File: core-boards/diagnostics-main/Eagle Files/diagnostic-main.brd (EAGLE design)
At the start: 79.2 x 84.8 mm, 50 parts, among them J1 A118090TR-ND, J2 3M15451-ND, J4 B2PS-VH(LF)(SN), Q1 16 MHz, U1 ATMEGA2560-16AU, U2 296-38653-1-ND, U3 MCP2551T-I/SN, U4 LM1085ISX-5.0/NOPB, U6 TXB0106PWR, U8 LP2985IM5X-3.3/NOPB, X1 22-23-2031, X2 B6B-EH-A(LF)(SN), X3 CC1101, X5 22-23-2031, X8 WM4803-ND

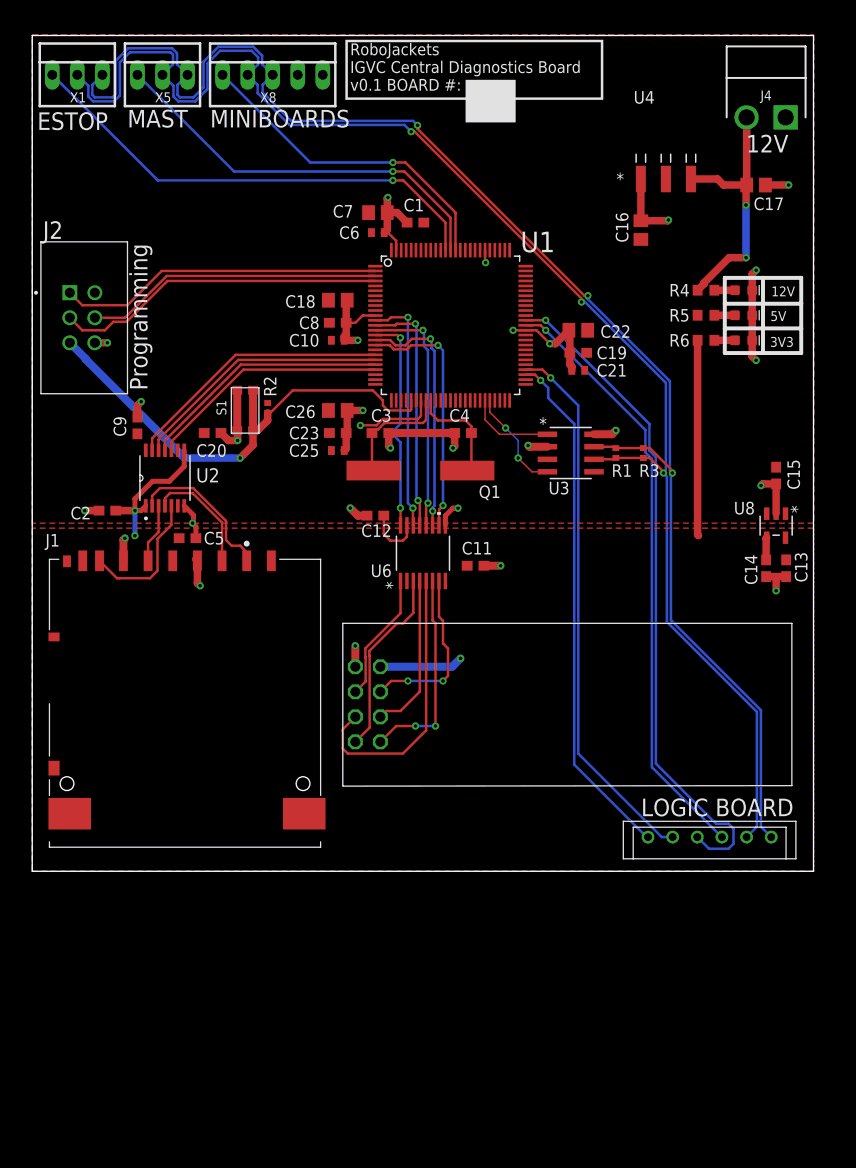
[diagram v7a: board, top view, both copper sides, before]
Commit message: Cleaning Up Parts Names and Part List
Still need to decide on connectors
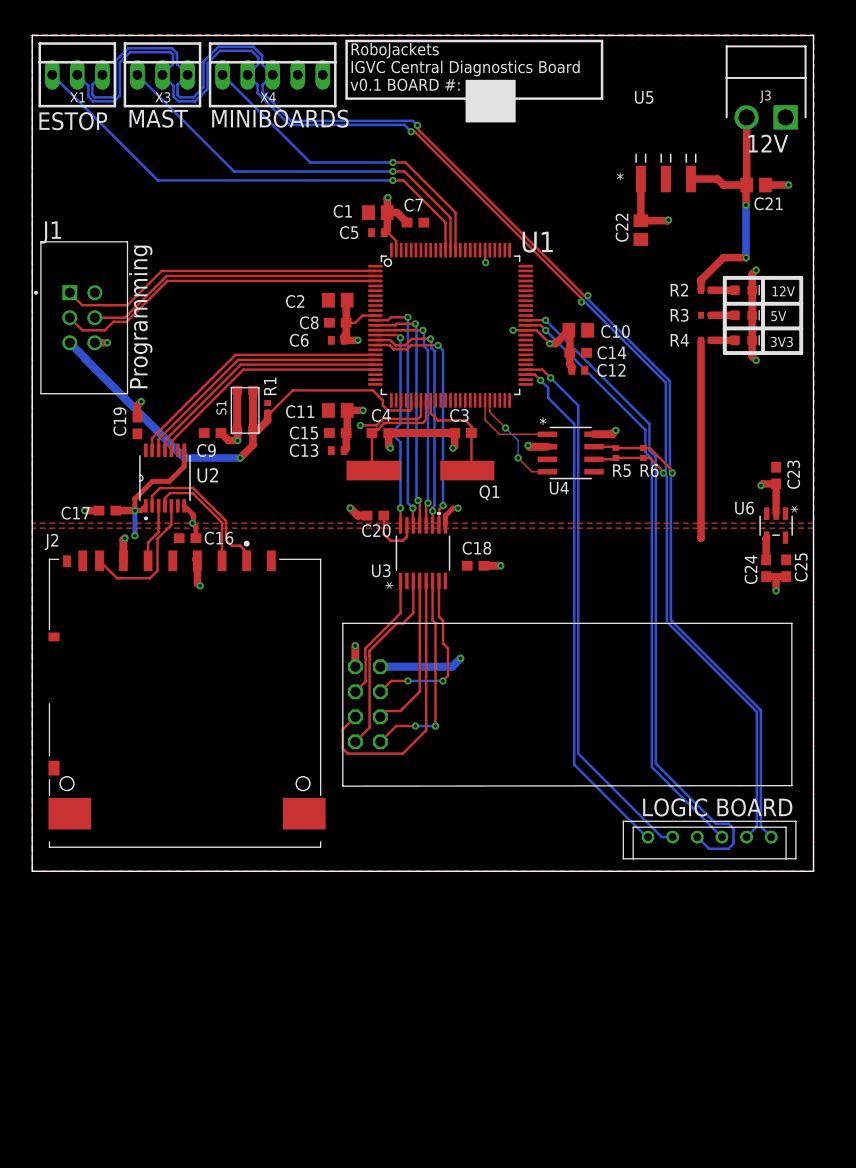
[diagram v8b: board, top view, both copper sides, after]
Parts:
- removed C26: 10uF, rcl:C0805
- removed U8: LP2985IM5X-3.3/NOPB, LP2985IM5X:MF05A
- added C24: .01uF, rcl:C0603
- added U5: LM1085ISX-5.0/NOPB, LM1085ISX:TS3B
- C1, C11, C2: value .1uF -> 10uF; device rcl:C0603 -> rcl:C0805
- C10, C21: value 1uF -> 10uF; device rcl:C0402 -> rcl:C0805
- C12, C5: value .1uF -> 1uF; device rcl:C0603 -> rcl:C0402
- C13: value 2.2uF -> 1uF; device rcl:C0603 -> rcl:C0402
- C14: value .01uF -> .1uF
- C15: value 1uF -> .1uF
- C16, C17, C18, C7: value 10uF -> .1uF; device rcl:C0805 -> rcl:C0603
- C23: value .1uF -> 1uF
- C25: value 1uF -> 2.2uF; device rcl:C0402 -> rcl:C0603
- J1: value A118090TR-ND -> 3M15451-ND; device A118090TR-ND:TE_1939870-1 -> 3M15451-ND:3M_30306-6002HB
- J2: value 3M15451-ND -> A118090TR-ND; device 3M15451-ND:3M_30306-6002HB -> A118090TR-ND:TE_1939870-1
- R1: value 120 -> 10k
- R2: value 10k -> 2.2k
- R3: value 120 -> 1k
- R4: value 2.2k -> 1k; device rcl:R0603 -> rcl:R0402
- R5, R6: value 1k -> 120; device rcl:R0603 -> rcl:R0402
- U3: value MCP2551T-I/SN -> TXB0106PWR; device MCP2551T:SOIC8-N_MC -> TXB0106PWR:PW16
- U4: value LM1085ISX-5.0/NOPB -> MCP2551T-I/SN; device LM1085ISX:TS3B -> MCP2551T:SOIC8-N_MC
- U6: value TXB0106PWR -> LP2985IM5X-3.3/NOPB; device TXB0106PWR:PW16 -> LP2985IM5X:MF05A
- X2: value B6B-EH-A(LF)(SN) -> CC1101; device IGVC-Connector:B6BEHALFSN -> IGVC-Connector:NRF24L01+PA+LNA
- X3: value CC1101 -> 22-23-2031; device IGVC-Connector:NRF24L01+PA+LNA -> con-molex:22-23-2031
- X5: value 22-23-2031 -> B6B-EH-A(LF)(SN); device con-molex:22-23-2031 -> IGVC-Connector:B6BEHALFSN
- moved X5 92.2 mm to (59.9, 16.5)
- moved X3 75.5 mm to (13.2, 96.0), turned to 0 degrees
- moved C17 73.6 mm to (7.62, 51.8), turned to 180 degrees
- moved C16 55.6 mm to (15.7, 49.0), turned to 0 degrees
- moved J1 51.1 mm to (3.81, 73.9)
- moved J2 51.1 mm to (15.5, 24.1)
- moved C13 47.0 mm to (31.0, 57.9), turned to 0 degrees
- moved C25 47.0 mm to (76.5, 46.0), turned to 270 degrees
- moved R2 46.0 mm to (68.3, 74.2), turned to 180 degrees
- moved C19 45.3 mm to (10.7, 60.5), turned to 90 degrees
- moved C15 44.7 mm to (31.0, 59.7), turned to 0 degrees
- moved C23 44.7 mm to (75.4, 55.4), turned to 270 degrees
- moved U4 37.3 mm to (54.6, 57.7)
- moved C5 36.5 mm to (35.1, 80.0)
- moved U6 35.9 mm to (75.4, 50.3), turned to 270 degrees
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- renumbered J4 to J3, X8 to X4
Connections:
- net !RESET: now also J1.5, R1.1; no longer J2.5, R2.1
- net +12V: now also C21.1, R2.2, U5.3; no longer C17.1, R4.2, U4.3
- net +3V3: now also C16.1, C17.1, C18.1, C25.1, J2.4, R4.2, U3.2, U3.8, U6.5, X2.VCC; no longer C11.1, C13.1, C2.1, C5.1, J1.4, R6.2, U6.2, U6.8, U8.5, X3.VCC
- net +5V: now also C11.1, C13.1, C14.1, C2.1, C5.1, J1.2, R1.2, R3.2, U3.15, U4.3, U5.2, U6.1, U6.3; no longer C16.1, C18.1, C21.1, C25.1, C26.1, J2.2, R2.2, R5.2, U3.3, U4.2, U6.15, U8.1, U8.3
- net 12V_LED_R: now also R2.1; no longer R4.1
- net 3V3_LED_R: now also R4.1; no longer R6.1
- net 5V_LED_R: now also R3.1; no longer R5.1
- net CAN_N: now also R5.1, R6.1, U4.6, X3.2, X5.X-5; no longer R1.1, R3.1, U3.6, X2.X-5, X5.2
- net CAN_P: now also R5.2, R6.2, U4.7, X3.3, X5.X-6; no longer R1.2, R3.2, U3.7, X2.X-6, X5.3
- net CAN_RX: now also U4.1; no longer U3.1
- net CAN_TX: now also U4.4; no longer U3.4
- net DIAG_RX: now also X5.X-4; no longer X2.X-4
- net DIAG_TX: now also X5.X-3; no longer X2.X-3
- net ENCODER1_SENSE: now also X5.X-1; no longer X2.X-1
- net ENCODER2_SENSE: now also X5.X-2; no longer X2.X-2
- net GND: now also C24.2, J2.3, U3.9, U4.2, U4.8, U5.1, U6.2, X2.GND; no longer C26.2, J1.3, U3.2, U3.8, U4.1, U6.9, U8.2, X3.GND
- net MAST_CONNECTED: now also X3.1; no longer X5.1
- net N$2: now also C24.1, U6.4; no longer C14.1, U8.4
- net PROGRAM_MISO: now also J1.1; no longer J2.1
- net PROGRAM_MOSI: now also J1.4; no longer J2.4
- net PROGRAM_SCK: now also J1.3; no longer J2.3
- net RADIO_CSN: now also U3.10; no longer U6.10
- net RADIO_CSN_3V3: now also U3.7, X2.CSN; no longer U6.7, X3.CSN
- net RADIO_IRQ: now also U3.11; no longer U6.11
- net RADIO_IRQ_3V3: now also U3.6, X2.IRQ; no longer U6.6, X3.IRQ
- net RADIO_MISO: now also U3.14; no longer U6.14
- net RADIO_MISO_3V3: now also U3.3, X2.MISO; no longer U6.3, X3.MISO
- net RADIO_MOSI: now also U3.13; no longer U6.13
- net RADIO_MOSI_3V3: now also U3.4, X2.MOSI; no longer U6.4, X3.MOSI
- net RADIO_SCK: now also U3.12; no longer U6.12
- net RADIO_SCK_3V3: now also U3.5, X2.SCK; no longer U6.5, X3.SCK
- net RADIO_SS: now also U3.16; no longer U6.16
- net RADIO_SS_3V3: now also U3.1, X2.CE; no longer U6.1, X3.CE
- net SD_MISO_3V3: now also J2.7; no longer J1.7
- net SD_MOSI_3V3: now also J2.2; no longer J1.2
- net SD_SCK_3V3: now also J2.5; no longer J1.5
- net SD_SS_3V3: now also J2.1; no longer J1.1
- net XTAL1: now also C3.2; no longer C4.2
- net XTAL2: now also C4.2; no longer C3.2
